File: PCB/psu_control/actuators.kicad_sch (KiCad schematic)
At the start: 22 parts

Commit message: psu_control v4 is completed
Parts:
- removed J?: Other 2 I2C, symbol Connector:Conn_01x03_Male
- removed M? (x2): 5V Fan, symbol Motor:Motor_DC
- added J9: Amplifier 2 I2C, Connector_JST:JST_PH_B3B-PH-K_1x03_P2.00mm_Vertical, symbol Connector:Conn_01x03_Male
- added M1, M2: Fan, Connector_JST:JST_PH_B2B-PH-K_1x02_P2.00mm_Vertical, symbol t-top:Fan
- C10, C8: renamed from C?; footprint (none) -> Capacitor_SMD:C_0805_2012Metric
- C9: renamed from C?; value 100µF/25V -> 100µF/35V; footprint (none) -> Capacitor_THT:CP_Radial_D6.3mm_P2.50mm
- D1, D2, D3: renamed from D?; footprint (none) -> Diode_SMD:D_SOD-123F
- J10, J7, J8: renamed from J?; footprint (none) -> Connector_JST:JST_PH_B3B-PH-K_1x03_P2.00mm_Vertical
- J6: renamed from J?; footprint (none) -> Connector_JST:JST_XH_B3B-XH-A_1x03_P2.50mm_Vertical
- LS1: renamed from LS?; footprint (none) -> t-top:WT-1205
- Q4: renamed from Q?; footprint (none) -> Package_SO:SOIC-8_3.9x4.9mm_P1.27mm
- R21, R22, R23, R24: renamed from R?; footprint (none) -> Resistor_SMD:R_0805_2012Metric
- RV1: renamed from RV?; footprint (none) -> Varistor:RV_Disc_D7mm_W4mm_P5mm
- gave numbers to parts that had none: 1
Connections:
- net GENERAL_SCL: now also J9.2 (Pin_2)
- net GENERAL_SDA: now also J9.3 (Pin_3)
- net GND: now also Q4.1 (S), Q4.3 (S), J9.1 (Pin_1); no longer Q4.1 (S), Q4.3 (S)
- net at D2.2 (A), LS1.2: now also Q4.7 (D), Q4.8 (D); no longer Q4.5 (D), Q4.6 (D)
- net at C10.1, C9.1, D1.1 (K)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: now also M1.2 (+), M2.2 (+)
- net at R21.2, R23.1: now also Q4.2 (G); no longer Q4.4 (G)
- net at R22.2, R24.1: now also Q4.4 (G); no longer Q4.2 (G)
- new net: D3.2 (A), M1.1 (-), M2.1 (-), Q4.5 (D), Q4.6 (D)
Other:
- note added: "J6: JST XH Connector"
- note added: "J7: JST PH Connector J8: JST PH Connector J9: JST PH Connector J10: JST PH Connector"
- note added: "M1: JST PH Connector M2: JST PH Connector"
- moved on the sheet: J10, J7, J8

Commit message: Update psu_control
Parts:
- J9: value Amplifier 2 I2C -> Other 2 I2C
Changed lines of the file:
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@@
       (effects (font (size 1.27 1.27)) (justify right))
     )
-    (property "Value" "Amplifier 2 I2C" (id 1) (at 82.55 110.4899 0)
+    (property "Value" "Other 2 I2C" (id 1) (at 82.55 110.4899 0)
       (effects (font (size 1.27 1.27)) (justify right))
     )

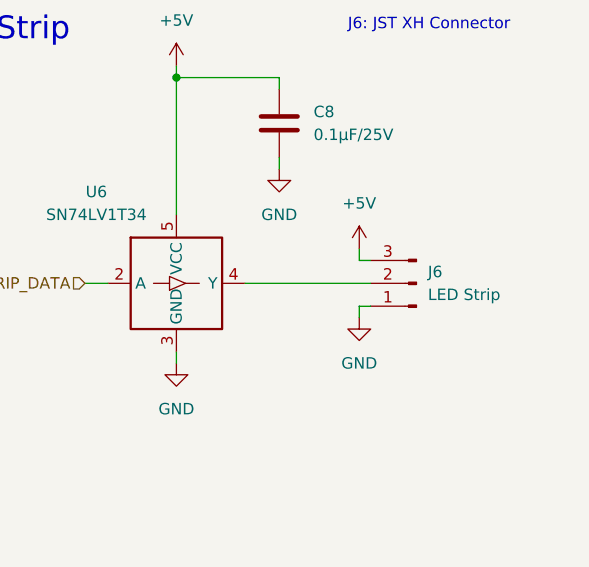
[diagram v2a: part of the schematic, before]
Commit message: Add output resistor for the led strip (data).
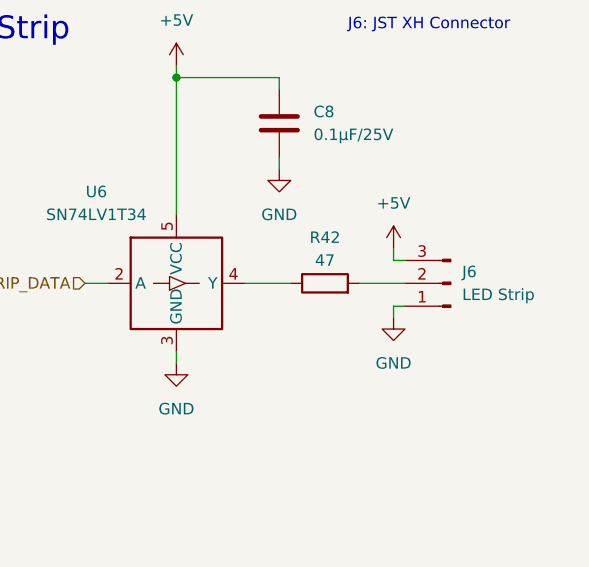
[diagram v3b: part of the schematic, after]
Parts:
- added R42: 47, Resistor_SMD:R_0805_2012Metric, symbol Device:R
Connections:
- net at J6.2 (Pin_2): now also R42.2; no longer U6.4 (Y)
- new net: R42.1, U6.4 (Y)
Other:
- moved on the sheet: J6
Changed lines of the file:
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@@
   (junction (at 110.49 48.26) (diameter 0) (color 0 0 0 0)
   )
-  (wire (pts (xy 250.19 43.18) (xy 264.16 43.18))
-    (stroke (width 0) (type default) (color 0 0 0 0))
-  )
   (polyline (pts (xy 102.87 114.3) (xy 102.87 120.65))
     (stroke (width 0) (type default) (color 0 0 0 0))
@@
     (stroke (width 0) (type default) (color 0 0 0 0))
   )
-  (wire (pts (xy 264.16 40.64) (xy 262.89 40.64))
+  (wire (pts (xy 267.97 40.64) (xy 266.7 40.64))
     (stroke (width 0) (type default) (color 0 0 0 0))
   )
@@
     (stroke (width 0) (type default) (color 0 0 0 0))
   )
-  (wire (pts (xy 264.16 45.72) (xy 262.89 45.72))
+  (wire (pts (xy 267.97 45.72) (xy 266.7 45.72))
     (stroke (width 0) (type default) (color 0 0 0 0))
   )
@@
     (stroke (width 0) (type default) (color 0 0 0 0))
   )
-  (wire (pts (xy 262.89 39.37) (xy 262.89 40.64))
+  (wire (pts (xy 266.7 39.37) (xy 266.7 40.64))
     (stroke (width 0) (type default) (color 0 0 0 0))
   )
@@
     (stroke (width 0) (type default) (color 0 0 0 0))
   )
+  (wire (pts (xy 262.89 43.18) (xy 267.97 43.18))
+    (stroke (width 0) (type default) (color 0 0 0 0))
+  )
   (wire (pts (xy 74.93 111.76) (xy 74.93 113.03))
     (stroke (width 0) (type default) (color 0 0 0 0))
@@
     (stroke (width 0) (type default) (color 0 0 0 0))
   )
+  (wire (pts (xy 250.19 43.18) (xy 255.27 43.18))
+    (stroke (width 0) (type default) (color 0 0 0 0))
+  )
   (wire (pts (xy 54.61 26.67) (xy 54.61 30.48))
     (stroke (width 0) (type default) (color 0 0 0 0))
@@
     (stroke (width 0) (type default) (color 0 0 0 0))
   )
-  (wire (pts (xy 262.89 45.72) (xy 262.89 46.99))
+  (wire (pts (xy 266.7 45.72) (xy 266.7 46.99))
     (stroke (width 0) (type default) (color 0 0 0 0))
   )
@@
     (pin "1")
   )
-  (symbol (lib_id "power:GND") (at 262.89 46.99 0) (unit 1)
-    (in_bom yes) (on_board yes) (fields_autoplaced)
-    (property "Reference" "#PWR0140" (id 0) (at 262.89 53.34 0)
-      (effects (font (size 1.27 1.27)) hide)
-    )
-    (property "Value" "GND" (id 1) (at 262.89 52.07 0))
-    (property "Footprint" "" (id 2) (at 262.89 46.99 0)
-      (effects (font (size 1.27 1.27)) hide)
-    )
-    (property "Datasheet" "" (id 3) (at 262.89 46.99 0)
+  (symbol (lib_id "power:GND") (at 266.7 46.99 0) (unit 1)
+    (in_bom yes) (on_board yes) (fields_autoplaced)
+    (property "Reference" "#PWR0140" (id 0) (at 266.7 53.34 0)
+      (effects (font (size 1.27 1.27)) hide)
+    )
+    (property "Value" "GND" (id 1) (at 266.7 52.07 0))
+    (property "Footprint" "" (id 2) (at 266.7 46.99 0)
+      (effects (font (size 1.27 1.27)) hide)
+    )
+    (property "Datasheet" "" (id 3) (at 266.7 46.99 0)
       (effects (font (size 1.27 1.27)) hide)
     )
@@
     (pin "1")
   )
-  (symbol (lib_id "Connector:Conn_01x03_Male") (at 269.24 43.18 180) (unit 1)
-    (in_bom yes) (on_board yes) (fields_autoplaced)
-    (property "Reference" "J6" (id 0) (at 270.51 41.9099 0)
-      (effects (font (size 1.27 1.27)) (justify right))
-    )
-    (property "Value" "LED Strip" (id 1) (at 270.51 44.4499 0)
-      (effects (font (size 1.27 1.27)) (justify right))
-    )
-    (property "Footprint" "Connector_JST:JST_XH_B3B-XH-A_1x03_P2.50mm_Vertical" (id 2) (at 269.24 43.18 0)
-      (effects (font (size 1.27 1.27)) hide)
-    )
-    (property "Datasheet" "~" (id 3) (at 269.24 43.18 0)
+  (symbol (lib_id "Connector:Conn_01x03_Male") (at 273.05 43.18 180) (unit 1)
+    (in_bom yes) (on_board yes) (fields_autoplaced)
+    (property "Reference" "J6" (id 0) (at 274.32 41.9099 0)
+      (effects (font (size 1.27 1.27)) (justify right))
+    )
+    (property "Value" "LED Strip" (id 1) (at 274.32 44.4499 0)
+      (effects (font (size 1.27 1.27)) (justify right))
+    )
+    (property "Footprint" "Connector_JST:JST_XH_B3B-XH-A_1x03_P2.50mm_Vertical" (id 2) (at 273.05 43.18 0)
+      (effects (font (size 1.27 1.27)) hide)
+    )
+    (property "Datasheet" "~" (id 3) (at 273.05 43.18 0)
       (effects (font (size 1.27 1.27)) hide)
     )
@@
     )
     (property "Datasheet" "~" (id 3) (at 168.91 59.69 0)
+      (effects (font (size 1.27 1.27)) hide)
+    )
+    (pin "1")
+    (pin "2")
+  )
+  (symbol (lib_id "Device:R") (at 259.08 43.18 90) (unit 1)
+    (in_bom yes) (on_board yes)
+    (property "Reference" "R42" (id 0) (at 259.08 38.1 90))
+    (property "Value" "47" (id 1) (at 259.08 40.64 90))
+    (property "Footprint" "Resistor_SMD:R_0805_2012Metric" (id 2) (at 259.08 44.958 90)
+      (effects (font (size 1.27 1.27)) hide)
+    )
+    (property "Datasheet" "~" (id 3) (at 259.08 43.18 0)
       (effects (font (size 1.27 1.27)) hide)
     )
@@
     (pin "6")
   )
-  (symbol (lib_id "power:+5V") (at 262.89 39.37 0) (unit 1)
-    (in_bom yes) (on_board yes) (fields_autoplaced)
-    (property "Reference" "#PWR0137" (id 0) (at 262.89 43.18 0)
-      (effects (font (size 1.27 1.27)) hide)
-    )
-    (property "Value" "+5V" (id 1) (at 262.89 34.29 0))
-    (property "Footprint" "" (id 2) (at 262.89 39.37 0)
-      (effects (font (size 1.27 1.27)) hide)
-    )
-    (property "Datasheet" "" (id 3) (at 262.89 39.37 0)
-      (effects (font (size 1.27 1.27)) hide)
-    )
+  (symbol (lib_id "power:+5V") (at 266.7 39.37 0) (unit 1)
+    (in_bom yes) (on_board yes) (fields_autoplaced)
+    (property "Reference" "#PWR0137" (id 0) (at 266.7 43.18 0)
+      (effects (font (size 1.27 1.27)) hide)
+    )
+    (property "Value" "+5V" (id 1) (at 266.7 34.29 0))
+    (property "Footprint" "" (id 2) (at 266.7 39.37 0)
+      (effects (font (size 1.27 1.27)) hide)
+    )
+    (property "Datasheet" "" (id 3) (at 266.7 39.37 0)
+      (effects (font (size 1.27 1.27)) hide)
+    )

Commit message: Fix PCBs.
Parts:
- removed C9: 100µF/35V, Capacitor_THT:CP_Radial_D6.3mm_P2.50mm, symbol Device:C_Polarized
- removed J10: Other 1 I2C, Connector_JST:JST_PH_B3B-PH-K_1x03_P2.00mm_Vertical, symbol Connector:Conn_01x03_Male
- removed J9: Other 2 I2C, Connector_JST:JST_PH_B3B-PH-K_1x03_P2.00mm_Vertical, symbol Connector:Conn_01x03_Male
- removed Q4: AO4818B, Package_SO:SOIC-8_3.9x4.9mm_P1.27mm, symbol t-top:AO4818B
- removed RV1: V12ZA1P, Varistor:RV_Disc_D7mm_W4mm_P5mm, symbol Device:Varistor
- added C24: 10µF/25V, Capacitor_SMD:C_0805_2012Metric, symbol Device:C
- added D6: SMAJ9.0A-13-F, Diode_SMD:D_SMA, symbol Device:D
- added Q4: DMG9926USD, Package_SO:SOIC-8_3.9x4.9mm_P1.27mm, symbol t-top:DMG9926USD
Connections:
- net GND: now also C24.2, Q4.1 (S), Q4.3 (S); no longer C10.2
- net at D2.2 (A), LS1.2: now also Q4.7 (D), Q4.8 (D)
- net at C10.1, D1.1 (K), D3.1 (K)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: now also C24.1, D6.1 (K)
- net at D3.2 (A), M1.1 (-), M2.1 (-): now also C10.2, D6.2 (A), Q4.5 (D), Q4.6 (D)
- net at R21.2, R23.1: now also Q4.2 (G)
- net at R22.2, R24.1: now also Q4.4 (G)
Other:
- note added: "J7: JST PH Connector J8: JST PH Connector"
- note removed: "J7: JST PH Connector J8: JST PH Connector J9: JST PH Connector J10: JST PH Connector"
